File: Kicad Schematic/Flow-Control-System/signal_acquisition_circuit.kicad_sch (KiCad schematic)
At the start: 45 parts, among them J10 receiver_signal_a, J11 emitter_signal_a, J12 emitter_signal_b, J5 GND, J6 +5V, J7 LF, J8 HF, J9 receiver_signal_b, U1 NE555P, U2 NE555P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

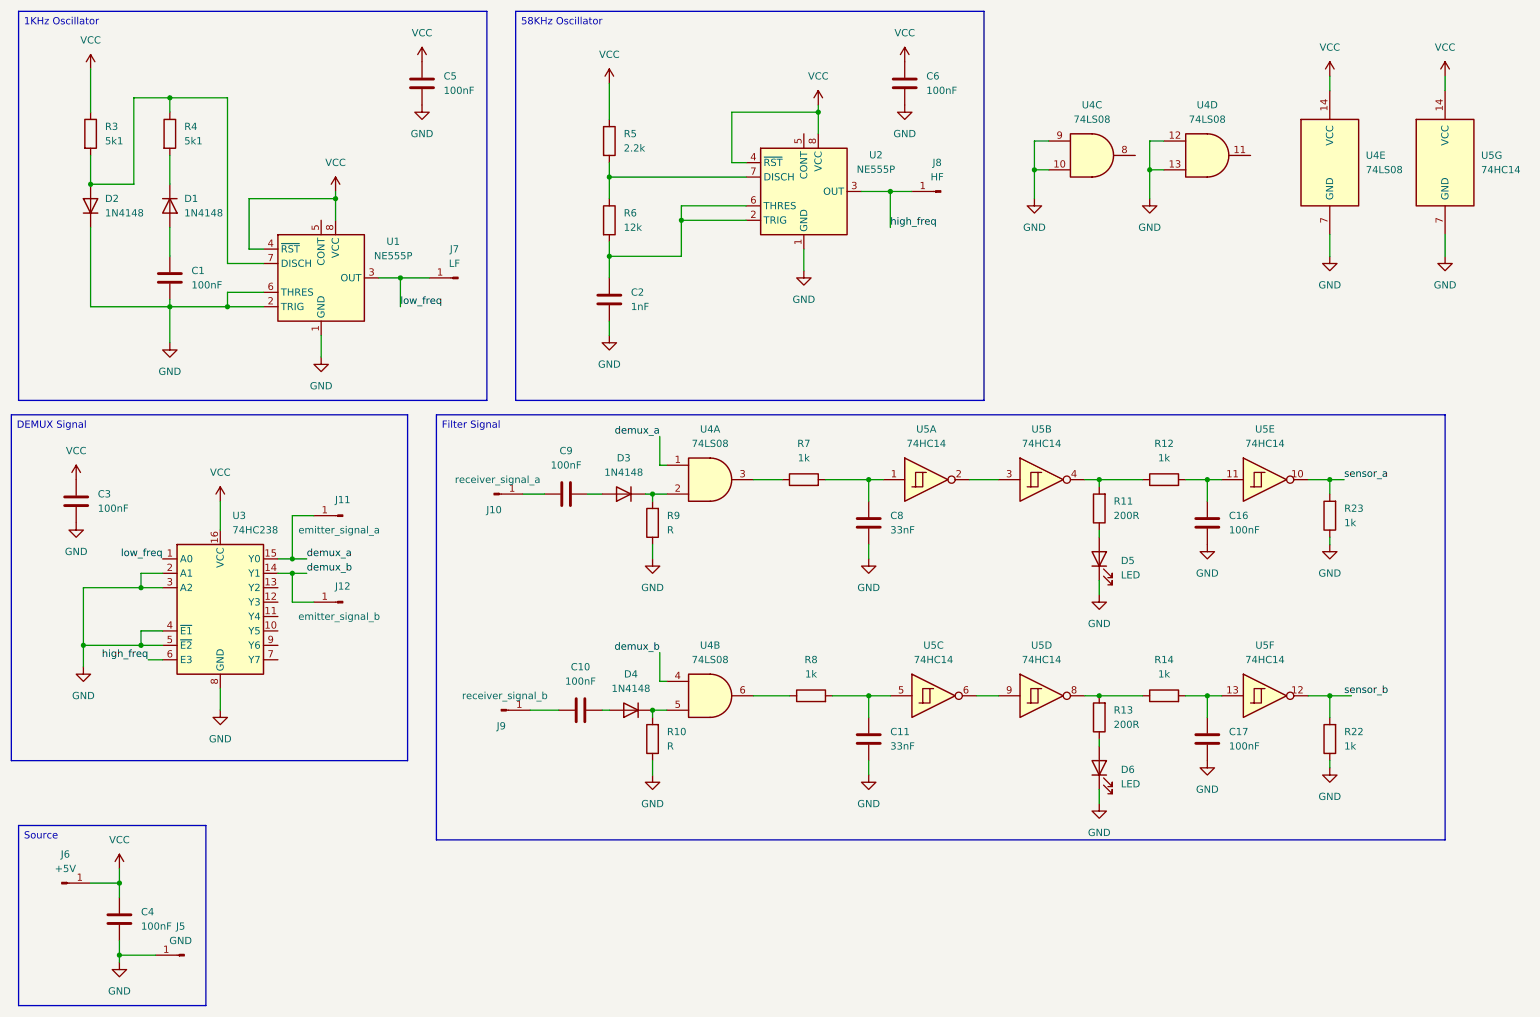
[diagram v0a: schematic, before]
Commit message: - ajuste no esquemático do Kicad, adicionado um buffer na entrada da AND do Schmitter para obter um buffer do receptor (TIL78), correção dos componentes do README.md e adicionado os componentes novos que foram usados no buffer
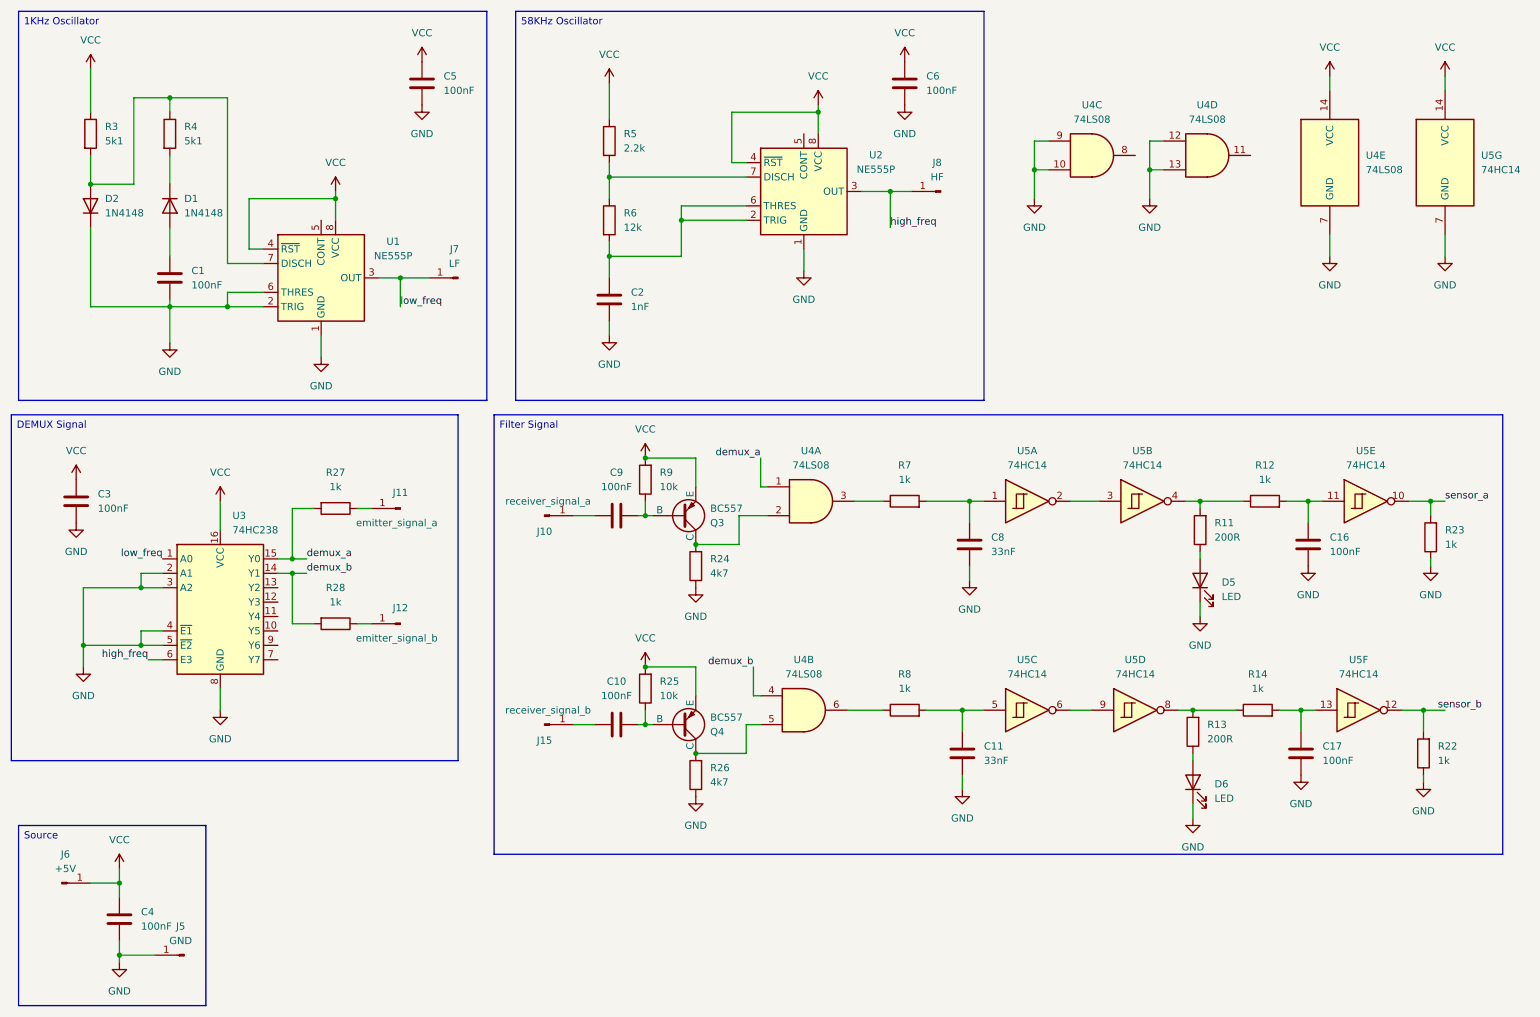
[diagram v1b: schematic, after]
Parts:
- removed D3, D4: 1N4148, Diode_THT:D_DO-35_SOD27_P7.62mm_Horizontal, symbol Diode:1N4148
- removed J9: receiver_signal_b, symbol Connector:Conn_01x01_Pin
- removed R10: R, symbol Device:R
- added J15: receiver_signal_b, symbol Connector:Conn_01x01_Pin
- added Q3, Q4: BC557, symbol Simulation_SPICE:PNP
- added R24, R26: 4k7, symbol Device:R
- added R25: 10k, symbol Device:R
- added R27, R28: 1k, symbol Device:R
- R9: value R -> 10k
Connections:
- net GND: now also R24.1, R26.1; no longer R9.1
- net VCC: now also R9.2, Q3.3 (E), Q4.3 (E), R25.2
- net demux_a: now also R27.2; no longer J11.1 (Pin_1)
- net demux_b: now also R28.2; no longer J12.1 (Pin_1)
- net at U4.5: now also Q4.1 (C), R26.2
- net at U4.2: now also Q3.1 (C), R24.2; no longer R9.2
- net at C10.1: now also J15.1 (Pin_1)
- net at C10.2: now also Q4.2 (B), R25.1
- net at C9.2: now also R9.1, Q3.2 (B)
- new net: J12.1 (Pin_1), R28.1
- new net: J11.1 (Pin_1), R27.1
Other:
- moved on the sheet: C11, C16, C17, C8, C9, D5, D6, J10, J11, J12, R11, R12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

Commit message: - ajuste do filtro passa-baixas da entrada das portas NOT Schmitt para não ocorrer a volta do sinal, além disso, adicionado um resistor de 100k como pull-down para descarregar o capacitor de filtro. - adicionado uma simulação LTSpice do low filter pass dos ajustes
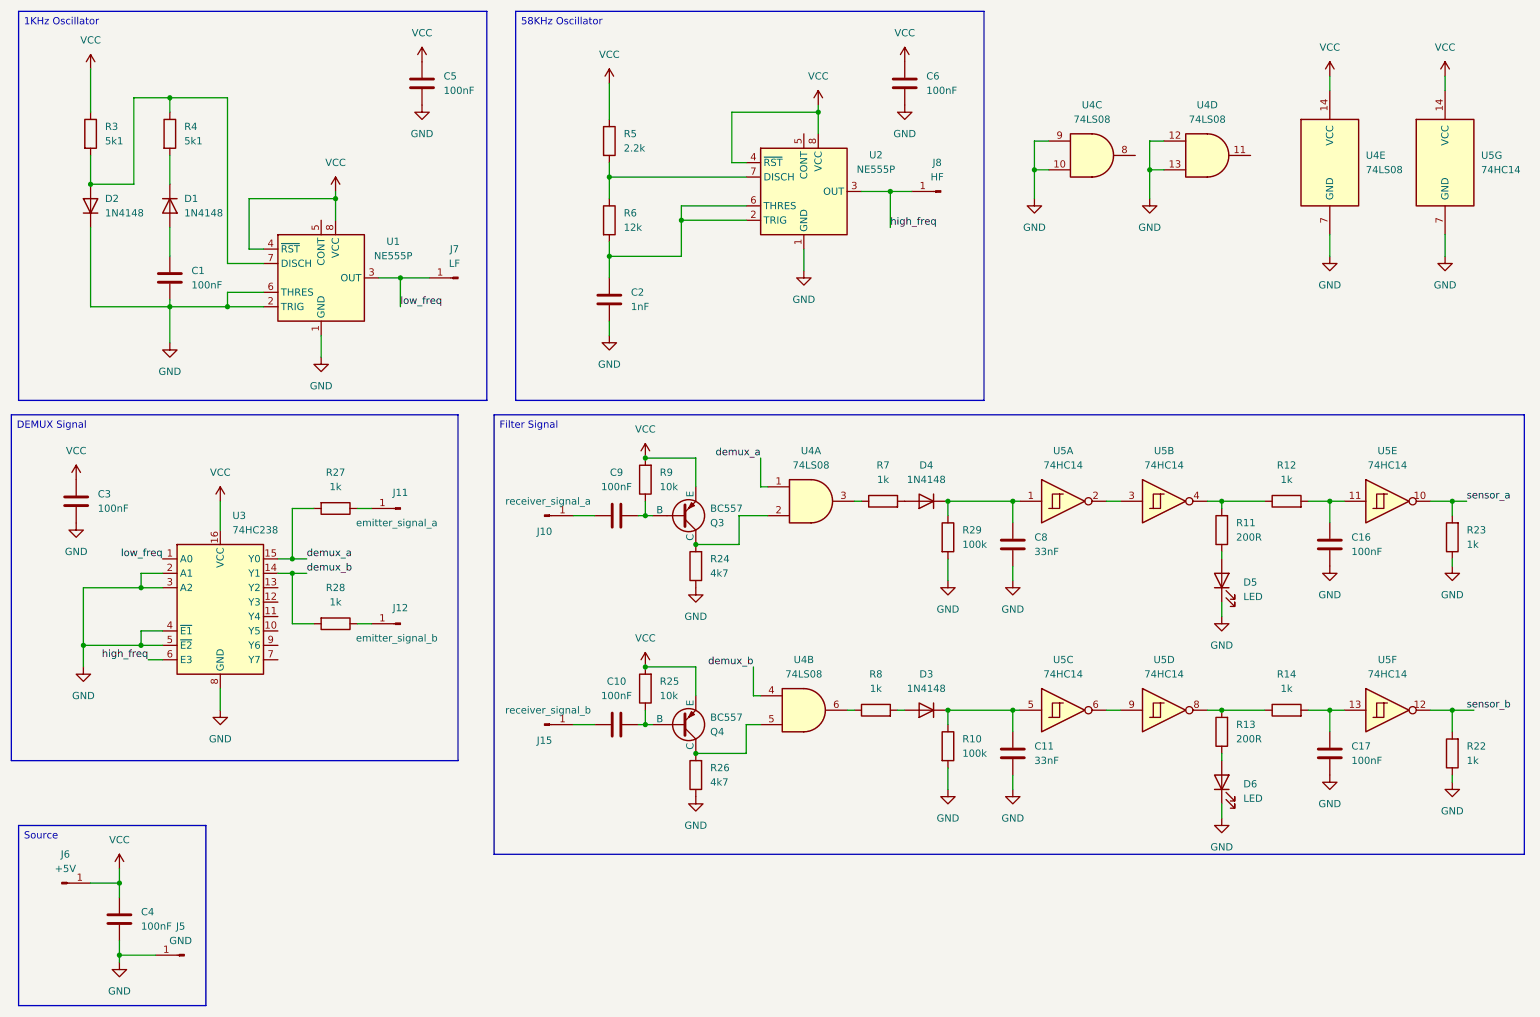
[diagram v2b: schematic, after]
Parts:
- added D3, D4: 1N4148, symbol Device:D
- added R10, R29: 100k, symbol Device:R
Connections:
- net GND: now also R10.2, R29.2
- net at C8.1, U5.1: now also D4.1 (K), R29.1; no longer R7.2
- net at C11.1, U5.5: now also D3.1 (K), R10.1; no longer R8.2
- new net: D4.2 (A), R7.2
- new net: D3.2 (A), R8.2
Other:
- moved on the sheet: C11, C16, C17, C8, D5, D6, R11, R12, R13, R14, R22, R23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

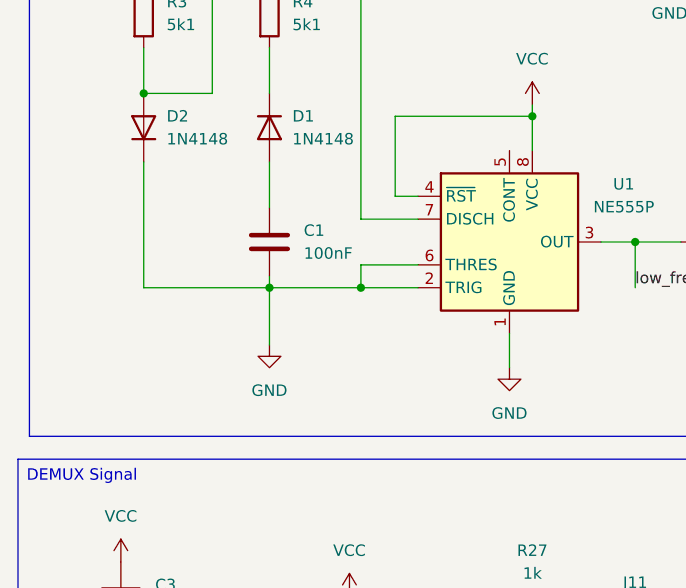
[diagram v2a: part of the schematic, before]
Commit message: - correção do esquemático do oscilador 58KHz
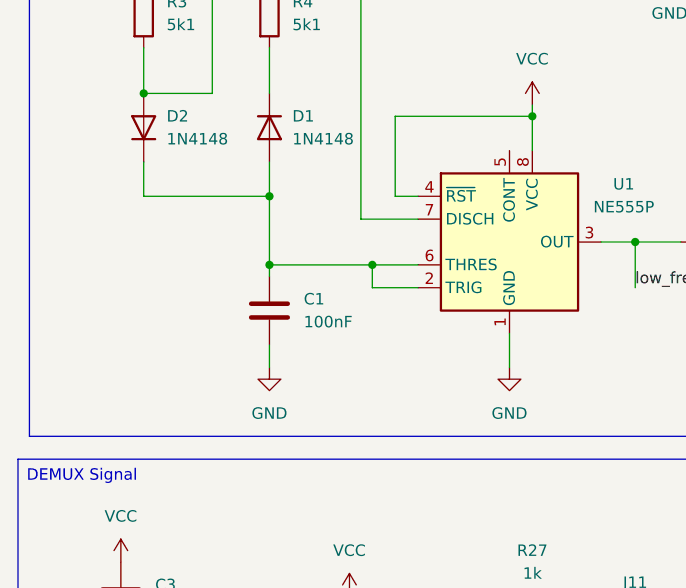
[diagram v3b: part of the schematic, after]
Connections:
- net GND: no longer D2.1 (K), U1.2 (TRIG), U1.6 (THRES)
- net at C1.1, D1.2 (A): now also D2.1 (K), U1.2 (TRIG), U1.6 (THRES)
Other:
- moved on the sheet: C1

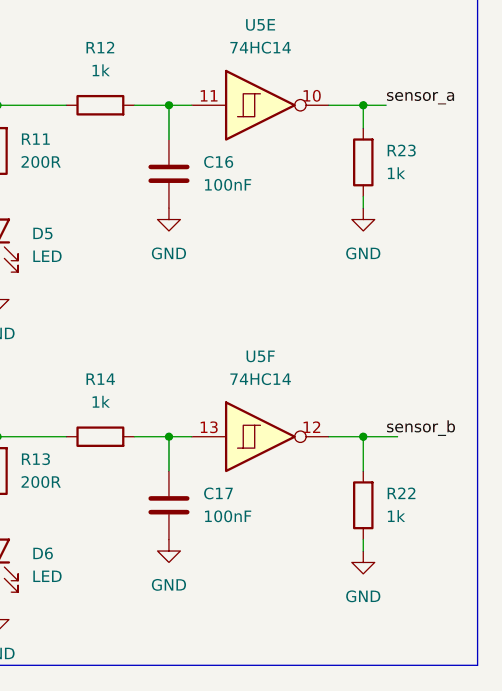
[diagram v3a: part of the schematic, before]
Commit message: - removido a inversora NOT da saída do 555, revertendo o equivoco do projeto - foi substituido os resistores de pull-down R23 e R22 de 1k para 10k
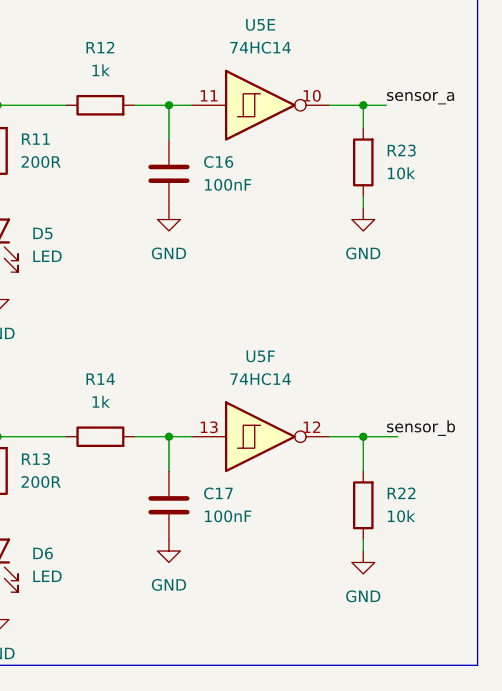
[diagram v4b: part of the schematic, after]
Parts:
- R22, R23: value 1k -> 10k
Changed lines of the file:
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@@
 			)
 		)
-		(property "Value" "1k"
+		(property "Value" "10k"
 			(at 273.05 148.5899 0)
 			(show_name no)
@@
 			)
 		)
-		(property "Value" "1k"
+		(property "Value" "10k"
 			(at 273.05 110.4899 0)
 			(show_name no)
